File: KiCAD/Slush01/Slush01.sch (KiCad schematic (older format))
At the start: 10 parts, among them IC1 ADR440ARMZ, J1 DB9F, J2 90122-0128, U1 LM78L05_SO8

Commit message: renamed Current_Source to Slush01 and added BOM
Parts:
- removed U1: LM78L05_SO8, Package_SO:SOIC-8_3.9x4.9mm_P1.27mm, symbol Regulator_Linear:LM78L05_SO8
- added IC14: LM78L05, Slush01:SOIC-8, symbol Slush01:LM78L05
- IC1: footprint Current_Source:SOP65P490X110-8N -> Slush01:MSOP-8; symbol Current_Source:ADR440ARMZ -> Slush01:ADR440ARMZ
- J1: footprint Current_Source:K202XHT-E9S-N -> Slush01:K202XHT-E9S-N; symbol Current_Source:DB9F -> Slush01:DB9F
- J2: footprint Current_Source:90122-0128 -> Slush01:90122-0128; symbol Current_Source:90122-0128 -> Slush01:90122-0128
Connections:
- wire segments 109 -> 100
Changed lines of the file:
@@
 EESchema Schematic File Version 4
+LIBS:Slush01-cache
 EELAYER 26 0
 EELAYER END
@@
 	3200 1550 3300 1550
 Wire Wire Line
-	3300 1550 3300 1750
-Wire Wire Line
-	3300 1750 3200 1750
-Wire Wire Line
-	3300 1750 3300 1950
-Wire Wire Line
-	3300 1950 3200 1950
-Connection ~ 3300 1750
-Wire Wire Line
-	3300 1950 3300 2050
-Wire Wire Line
-	3300 2050 3200 2050
-Connection ~ 3300 1950
-Wire Wire Line
 	3200 1650 3400 1650
 $Comp
@@
 F9 "1Vin" I R 4450 3300 60
 $EndSheet
-Wire Wire Line
-	3300 2050 3300 2500
-Connection ~ 3300 2050
 $Comp
 L power:GND #PWR03
@@
 	4700 3150 4450 3150
 Connection ~ 4700 3150
-$Comp
-L Regulator_Linear:LM78L05_SO8 U1
-U 1 1 5D69F559
-P 4250 1450
-F 0 "U1" H 4250 1692 50  0000 C CNN
-F 1 "LM78L05_SO8" H 4250 1601 50  0000 C CNN
-F 2 "Package_SO:SOIC-8_3.9x4.9mm_P1.27mm" H 4350 1650 50  0001 C CIN
-F 3 "http://www.fairchildsemi.com/ds/LM/LM78L05A.pdf" H 4450 1450 50  0001 C CNN
-	1    4250 1450
-	1    0    0    -1
-$EndComp
 Wire Wire Line
 	4250 1750 4250 1800
@@
 	2250 6000 2750 6000
 Wire Wire Line
-	2900 2450 2900 2500
-Wire Wire Line
-	2900 2500 3300 2500
-Connection ~ 3300 2500
-Wire Wire Line
-	3300 2500 3300 2550
-Wire Wire Line
 	1850 4050 1950 4050
 Wire Wire Line
@@
 	5850 3350 5850 3550
 $Comp
-L Current_Source:ADR440ARMZ IC1
+L Slush01:ADR440ARMZ IC1
 U 1 1 5D42964B
 P 5850 3050
 F 0 "IC1" H 6350 3317 50  0000 C CNN
 F 1 "ADR440ARMZ" H 6350 3226 50  0000 C CNN
-F 2 "Current_Source:SOP65P490X110-8N" H 6350 2500 50  0001 C CNN
+F 2 "Slush01:MSOP-8" H 6350 2500 50  0001 C CNN
 F 3 "http://docs-europe.electrocomponents.com/webdocs/0de0/0900766b80de0ad0.pdf" H 6350 2400 50  0001 C CNN
 F 4 "V-Ref Precision 2.048V 10mA 8-Pin MSOP" H 6350 2300 50  0001 C CNN "Description"
@@
 $EndComp
 $Comp
-L Current_Source:DB9F J1
+L Slush01:DB9F J1
 U 1 1 5D42E11B
 P 2900 1850
 F 0 "J1" H 2820 2542 50  0000 C CNN
 F 1 "DB9F" H 2820 2451 50  0000 C CNN
-F 2 "Current_Source:K202XHT-E9S-N" H 2900 1850 50  0001 C CNN
+F 2 "Slush01:K202XHT-E9S-N" H 2900 1850 50  0001 C CNN
 F 3 "" H 2900 1850 50  0001 C CNN
 	1    2900 1850
@@
 $EndComp
 $Comp
-L Current_Source:90122-0128 J2
+L Slush01:90122-0128 J2
 U 1 1 5D72D6A3
 P 1500 5600
 F 0 "J2" H 1681 7375 50  0000 C CNN
 F 1 "90122-0128" H 1681 7284 50  0000 C CNN
-F 2 "Current_Source:90122-0128" H 1650 6000 50  0001 C CNN
+F 2 "Slush01:90122-0128" H 1650 6000 50  0001 C CNN
 F 3 "" H 1650 6000 50  0001 C CNN
 	1    1500 5600
@@
 $EndComp
 $Comp
-L power:GNDA #PWR?
+L power:GNDA #PWR0101
 U 1 1 5D44ABAD
 P 4600 6600
-AR Path="/5D44ABAD" Ref="#PWR?"  Part="1"
+AR Path="/5D44ABAD" Ref="#PWR0101"  Part="1"
 AR Path="/59ED0E6A/5D44ABAD" Ref="#PWR?"  Part="1"
-F 0 "#PWR?" H 4600 6350 50  0001 C CNN
+F 0 "#PWR0101" H 4600 6350 50  0001 C CNN
 F 1 "GNDA" H 4605 6427 50  0000 C CNN
 F 2 "" H 4600 6600 50  0001 C CNN
@@
 	1    0    0    -1
 $EndComp
+Wire Wire Line
+	3300 1550 3300 2550
+$Comp
+L Slush01:LM78L05 IC14
+U 1 1 5D43B63A
+P 4250 1500
+F 0 "IC14" H 4250 1792 50  0000 C CNN
+F 1 "LM78L05" H 4250 1701 50  0000 C CNN
+F 2 "Slush01:SOIC-8" H 4250 1800 50  0001 C CNN
+F 3 "" H 4250 1800 50  0001 C CNN
+	1    4250 1500
+	1    0    0    -1
+$EndComp

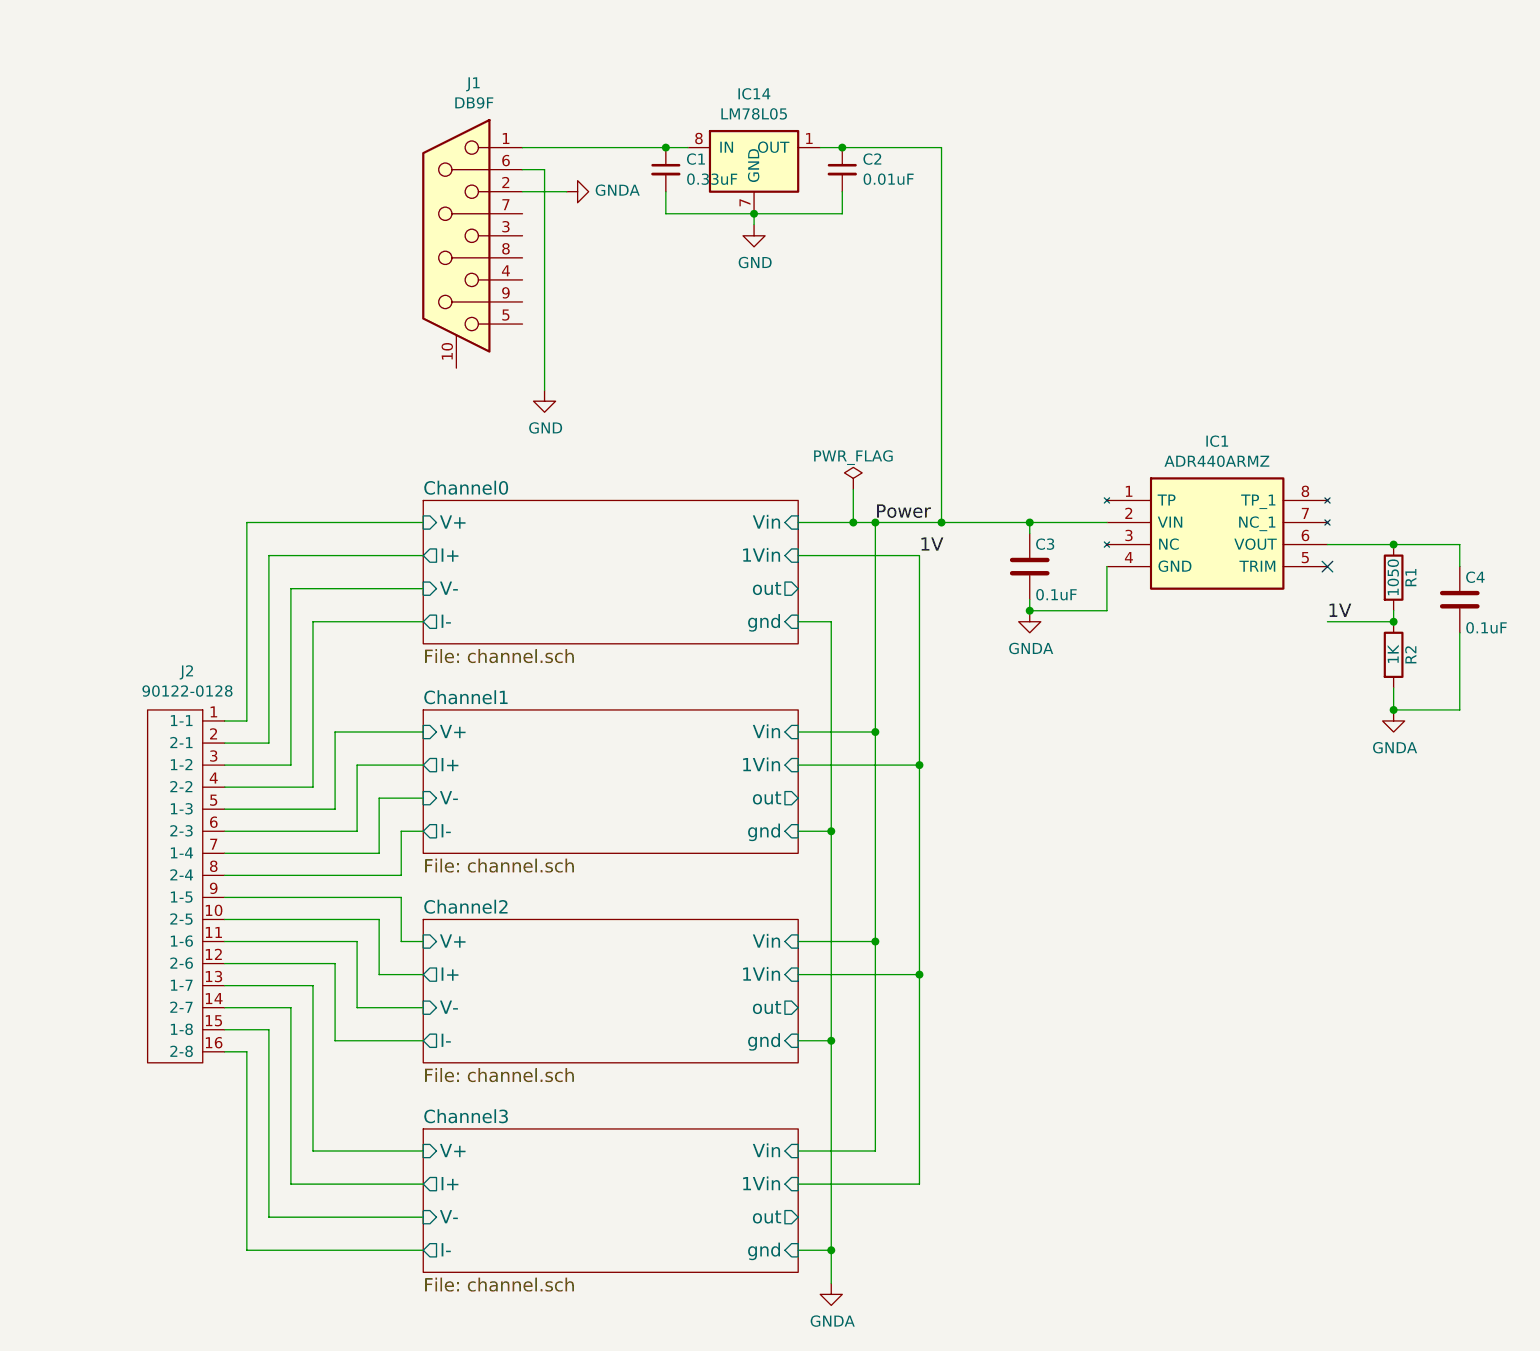
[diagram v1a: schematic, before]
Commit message: added ADC to Slush01
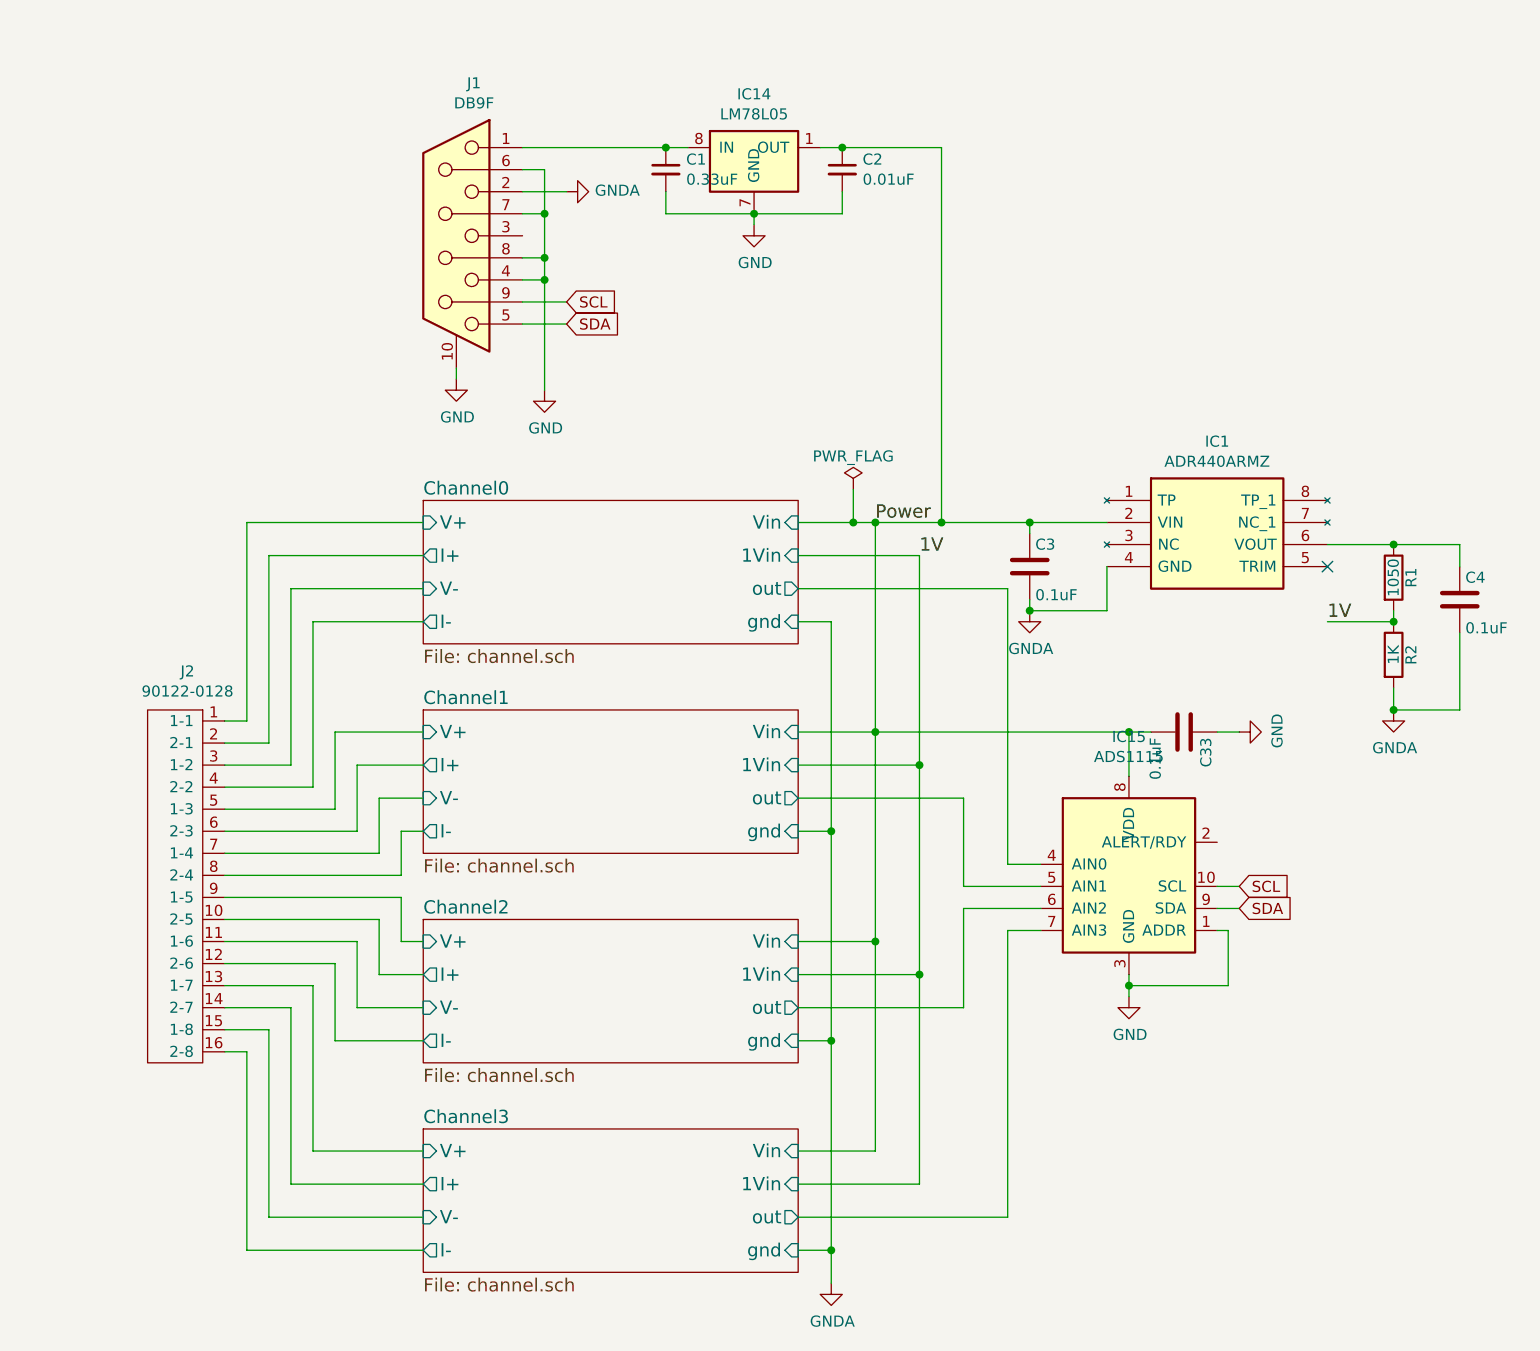
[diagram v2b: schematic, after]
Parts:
- added C33: 0.1uF, Capacitor_SMD:C_0805_2012Metric_Pad1.15x1.40mm_HandSolder, symbol Device:C
- added IC15: ADS1115, Slush01:VSSOP-10, symbol Slush01:ADS1115
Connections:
- net Channel0/out: now also IC15.4 (AIN0)
- net Channel1/out: now also IC15.5 (AIN1)
- net Channel2/out: now also IC15.6 (AIN2)
- net Channel3/out: now also IC15.7 (AIN3)
- net GND: now also J1.10 (PAD), J1.4, J1.7, J1.8, C33.1, IC15.1 (ADDR), IC15.3 (GND)
- net Power: now also C33.2, IC15.8 (VDD)
- net SDA: now reaches J1.5
- net SDA: now also IC15.9 (SDA)
- net SCL: now reaches J1.9
- net SCL: now also IC15.10 (SCL)
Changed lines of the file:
@@
 EESchema Schematic File Version 4
-LIBS:Slush01-cache
 EELAYER 26 0
 EELAYER END
@@
 $EndComp
 Wire Wire Line
-	3300 1550 3300 2550
+	3300 1550 3300 1750
 $Comp
 L Slush01:LM78L05 IC14
@@
 	1    0    0    -1
 $EndComp
+$Comp
+L Slush01:ADS1115 IC15
+U 1 1 5D449C03
+P 5950 4750
+F 0 "IC15" H 5950 5378 50  0000 C CNN
+F 1 "ADS1115" H 5950 5287 50  0000 C CNN
+F 2 "Slush01:VSSOP-10" H 5950 4750 50  0001 C CNN
+F 3 "" H 5950 4750 50  0001 C CNN
+	1    5950 4750
+	1    0    0    -1
+$EndComp
+Wire Wire Line
+	4450 4400 5200 4400
+Wire Wire Line
+	4450 5350 5200 5350
+Wire Wire Line
+	5200 4800 5550 4800
+Wire Wire Line
+	5200 4400 5200 4800
+Wire Wire Line
+	5200 4900 5550 4900
+Wire Wire Line
+	5200 4900 5200 5350
+Wire Wire Line
+	4450 6300 5400 6300
+Wire Wire Line
+	5400 6300 5400 5000
+Wire Wire Line
+	5400 5000 5550 5000
+Wire Wire Line
+	4450 3450 5400 3450
+Wire Wire Line
+	5400 3450 5400 4700
+Wire Wire Line
+	5400 4700 5550 4700
+Wire Wire Line
+	5950 4300 5950 4100
+Wire Wire Line
+	5950 4100 4800 4100
+$Comp
+L power:GND #PWR0150
+U 1 1 5D46966C
+P 5950 5300
+F 0 "#PWR0150" H 5950 5050 50  0001 C CNN
+F 1 "GND" H 5955 5127 50  0000 C CNN
+F 2 "" H 5950 5300 50  0001 C CNN
+F 3 "" H 5950 5300 50  0001 C CNN
+	1    5950 5300
+	1    0    0    -1
+$EndComp
+Wire Wire Line
+	5950 5300 5950 5250
+Wire Wire Line
+	3200 2150 3400 2150
+Wire Wire Line
+	3200 2250 3400 2250
+Text GLabel 3400 2150 2    50   Input ~ 0
+SCL
+Text GLabel 3400 2250 2    50   Input ~ 0
+SDA
+Wire Wire Line
+	6350 4800 6450 4800
+Wire Wire Line
+	6350 4900 6450 4900
+Text GLabel 6450 4800 2    50   Input ~ 0
+SCL
+Text GLabel 6450 4900 2    50   Input ~ 0
+SDA
+$Comp
+L Device:C C33
+U 1 1 5D481DEB
+P 6200 4100
+F 0 "C33" H 6225 4200 50  0000 L CNN
+F 1 "0.1uF" H 6225 4000 50  0000 L TNN
+F 2 "Capacitor_SMD:C_0805_2012Metric_Pad1.15x1.40mm_HandSolder" H 6238 3950 50  0001 C CNN
+F 3 "" H 6200 4100 50  0001 C CNN
+F 4 "-" H -1350 700 50  0001 C CNN "MFR"
+F 5 "-" H -1350 700 50  0001 C CNN "MPN"
+F 6 "-" H -1350 700 50  0001 C CNN "SPR"
+F 7 "-" H -1350 700 50  0001 C CNN "SPN"
+F 8 "-" H -1350 700 50  0001 C CNN "SPURL"
+	1    6200 4100
+	0    1    1    0
+$EndComp
+Wire Wire Line
+	6050 4100 5950 4100
+Connection ~ 5950 4100
+Wire Wire Line
+	6350 4100 6450 4100
+$Comp
+L power:GND #PWR0151
+U 1 1 5D48A776
+P 6450 4100
+F 0 "#PWR0151" H 6450 3850 50  0001 C CNN
+F 1 "GND" H 6455 3927 50  0000 C CNN
+F 2 "" H 6450 4100 50  0001 C CNN
+F 3 "" H 6450 4100 50  0001 C CNN
+	1    6450 4100
+	0    -1   -1   0
+$EndComp
+Wire Wire Line
+	6350 5000 6400 5000
+Wire Wire Line
+	6400 5000 6400 5250
+Wire Wire Line
+	6400 5250 5950 5250
+Connection ~ 5950 5250
+Wire Wire Line
+	5950 5250 5950 5200
+Wire Wire Line
+	2900 2450 2900 2500
+$Comp
+L power:GND #PWR0152
+U 1 1 5D49CEC6
+P 2900 2500
+F 0 "#PWR0152" H 2900 2250 50  0001 C CNN
+F 1 "GND" H 2905 2327 50  0000 C CNN
+F 2 "" H 2900 2500 50  0001 C CNN
+F 3 "" H 2900 2500 50  0001 C CNN
+	1    2900 2500
+	1    0    0    -1
+$EndComp
+Wire Wire Line
+	3200 1750 3300 1750
+Connection ~ 3300 1750
+Wire Wire Line
+	3300 1750 3300 1950
+Wire Wire Line
+	3200 1950 3300 1950
+Connection ~ 3300 1950
+Wire Wire Line
+	3300 1950 3300 2050
+Wire Wire Line
+	3200 2050 3300 2050
+Connection ~ 3300 2050
+Wire Wire Line
+	3300 2050 3300 2550
 $EndSCHEMATC
